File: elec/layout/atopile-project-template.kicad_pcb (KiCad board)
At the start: 2 copper layers, 1 part

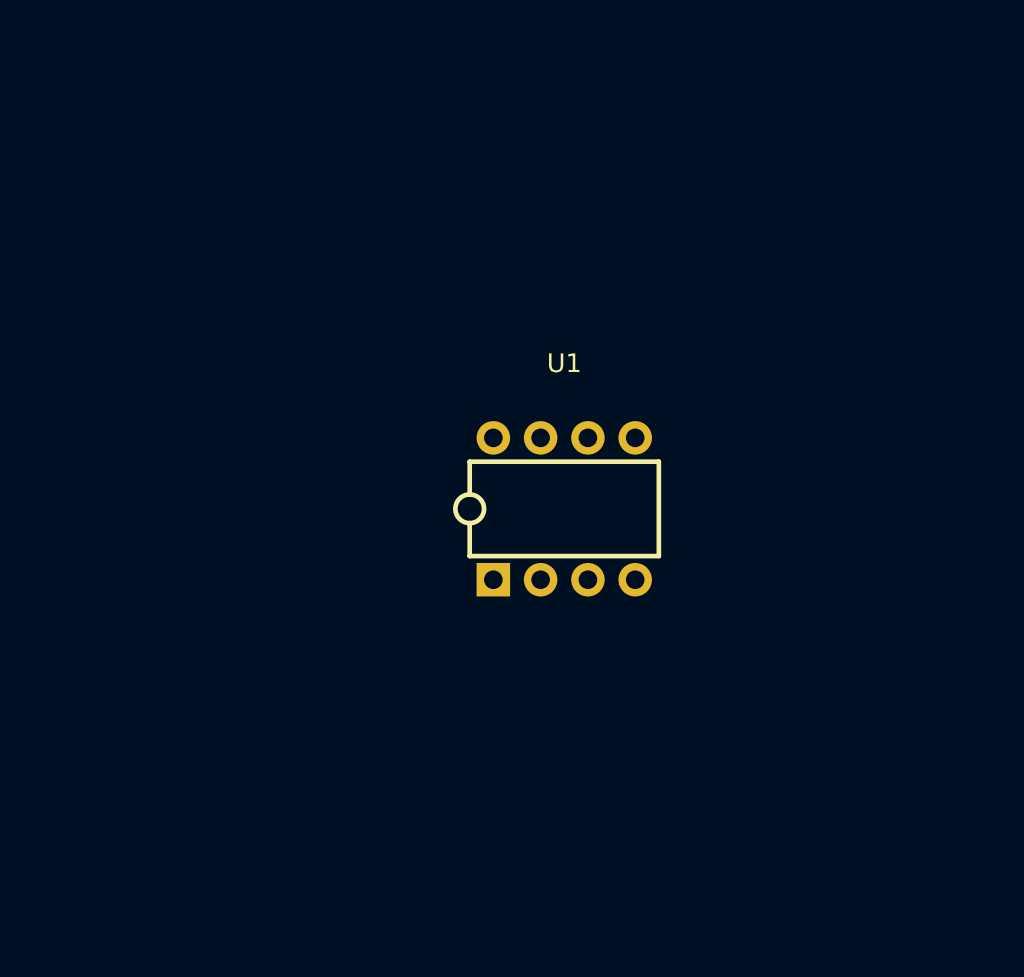
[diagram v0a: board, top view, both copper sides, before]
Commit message: added a few more comments, added a cap so we can show connections, modified kicad project lib path as it was broken
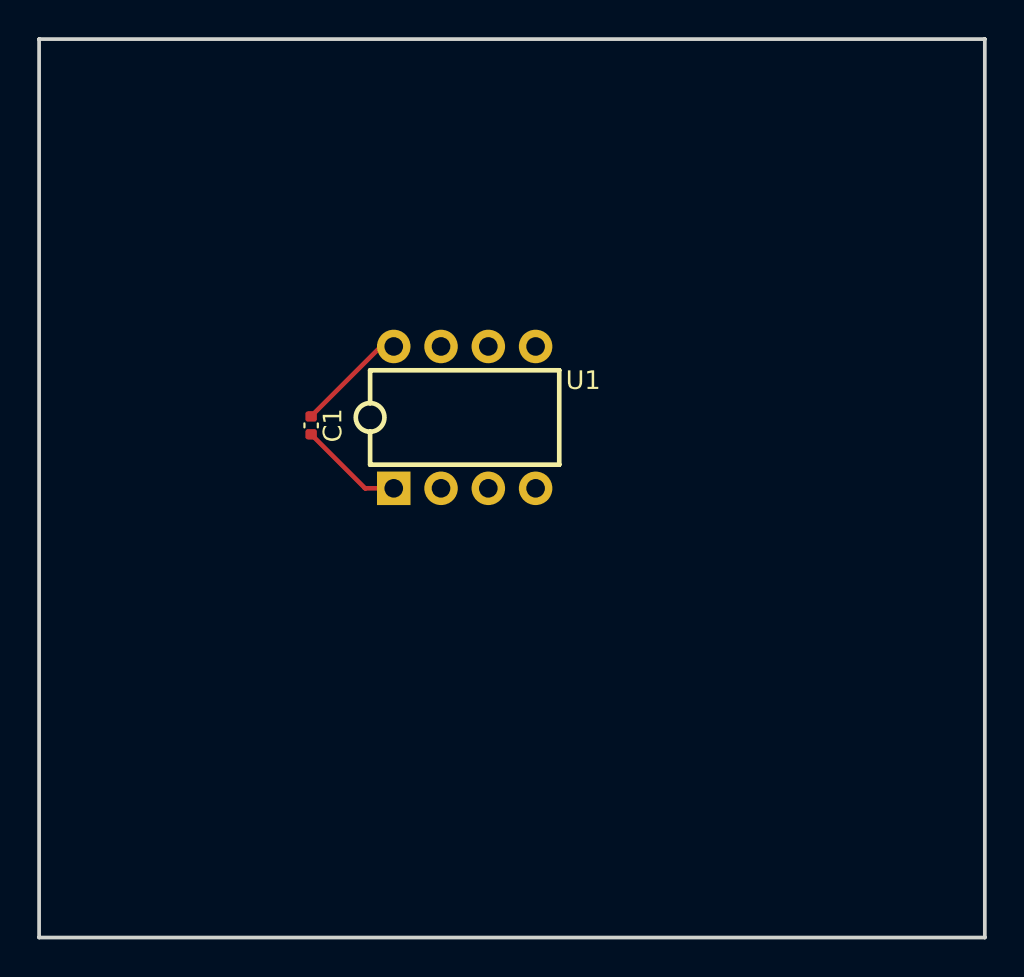
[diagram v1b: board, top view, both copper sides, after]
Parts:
- added C1: 100nF, Capacitor_SMD:C_0402_1005Metric, F.Cu at (134.0, 94.4)
- moved U1 7.26 mm to (142.2, 94.0)
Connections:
- U1 pad 1: Timer555-gnd -> HelloWorld-gnd
- U1 pad 8: Timer555-vcc_5v -> HelloWorld-vcc_5v
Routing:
- net HelloWorld-vcc_5v: track 0.00 -> 6.00 mm
- net HelloWorld-gnd: track 0.00 -> 5.64 mm
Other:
- board outline added: 50.8 x 48.3 mm
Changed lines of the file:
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@@
   )
   (net 0 "")
-  (net 1 "Timer555-gnd")
-  (net 2 "timer-trigger")
-  (net 3 "timer-output")
-  (net 4 "timer-reset")
-  (net 5 "timer-ctrl_v")
-  (net 6 "timer-threshold")
-  (net 7 "timer-discharge")
-  (net 8 "Timer555-vcc_5v")
+  (net 1 "HelloWorld-vcc_5v")
+  (net 2 "HelloWorld-gnd")
+  (net 3 "timer-trigger")
+  (net 4 "timer-output")
+  (net 5 "timer-reset")
+  (net 6 "timer-ctrl_v")
+  (net 7 "timer-threshold")
+  (net 8 "timer-discharge")
   (footprint "lib:DIP-8_L9.7-W6.4-P2.54-LS7.6-BL" (layer "F.Cu")
-    (at 147.59 98.89)
+    (at 142.24 93.98)
     (attr smd)
-    (fp_text reference "U1" (at 0 -7.81) (layer "F.SilkS")
+    (fp_text reference "U1" (at 6.363769 -1.989911) (layer "F.SilkS")
         (effects (font (size 1 1) (thickness 0.15)))
     )
@@
     (fp_line (start 5.08 2.54) (end 5.08 -2.53)
       (stroke (width 0.25) (type solid)) (layer "F.SilkS"))
-    (fp_arc (start -5.093438 0.769883) (mid -5.073311 -0.769971) (end -5.08 0.77)
+    (fp_arc (start -5.093438 0.769883) (mid -5.073281 -0.769971) (end -5.08 0.77)
       (stroke (width 0.25) (type solid)) (layer "F.SilkS"))
     (fp_circle (center -3.94 4.45) (end -3.64 4.45)
@@
       (stroke (width 0.06) (type solid)) (fill none) (layer "F.Fab"))
     (pad "1" thru_hole rect (at -3.81 3.81) (size 1.8 1.8) (drill 0.999998) (layers "*.Cu" "*.Mask")
-      (net 1 "Timer555-gnd"))
+      (net 2 "HelloWorld-gnd"))
     (pad "2" thru_hole circle (at -1.27 3.81) (size 1.8 1.8) (drill 0.999998) (layers "*.Cu" "*.Mask")
-      (net 2 "timer-trigger"))
+      (net 3 "timer-trigger"))
     (pad "3" thru_hole circle (at 1.27 3.81) (size 1.8 1.8) (drill 0.999998) (layers "*.Cu" "*.Mask")
-      (net 3 "timer-output"))
+      (net 4 "timer-output"))
     (pad "4" thru_hole circle (at 3.81 3.81) (size 1.8 1.8) (drill 0.999998) (layers "*.Cu" "*.Mask")
-      (net 4 "timer-reset"))
+      (net 5 "timer-reset"))
     (pad "5" thru_hole circle (at 3.81 -3.81) (size 1.8 1.8) (drill 0.999998) (layers "*.Cu" "*.Mask")
-      (net 5 "timer-ctrl_v"))
+      (net 6 "timer-ctrl_v"))
     (pad "6" thru_hole circle (at 1.27 -3.81) (size 1.8 1.8) (drill 0.999998) (layers "*.Cu" "*.Mask")
-      (net 6 "timer-threshold"))
+      (net 7 "timer-threshold"))
     (pad "7" thru_hole circle (at -1.27 -3.81) (size 1.8 1.8) (drill 0.999998) (layers "*.Cu" "*.Mask")
-      (net 7 "timer-discharge"))
+      (net 8 "timer-discharge"))
     (pad "8" thru_hole circle (at -3.81 -3.81) (size 1.8 1.8) (drill 0.999998) (layers "*.Cu" "*.Mask")
-      (net 8 "Timer555-vcc_5v"))
+      (net 1 "HelloWorld-vcc_5v"))
     (model "./lib/lib.3dshapes/DIP-8_L9.8-W6.6-H3.5-LS7.62-P2.54.wrl"
       (offset (xyz 0 -0 3))
@@
     )
   )
+  (footprint "Capacitor_SMD:C_0402_1005Metric" (layer "F.Cu")
+    (at 133.991711 94.410054 -90)
+    (descr "Capacitor SMD 0402 (1005 Metric), square (rectangular) end terminal, IPC_7351 nominal, (Body size source: IPC-SM-782 page 76, https://www.pcb-3d.com/wordpress/wp-content/uploads/ipc-sm-782a_amendment_1_and_2.pdf), generated with kicad-footprint-generator")
+    (tags "capacitor")
+    (attr smd)
+    (fp_text reference "C1" (at 0 -1.16 90) (layer "F.SilkS")
+        (effects (font (size 1 1) (thickness 0.15)))
+    )
+    (fp_text value "100nF" (at 0 1.16 90) (layer "F.Fab")
+        (effects (font (size 1 1) (thickness 0.15)))
+    )
+    (fp_text user "${REFERENCE}" (at 0 0 90) (layer "F.Fab")
+        (effects (font (size 0.25 0.25) (thickness 0.04)))
+    )
+    (fp_line (start -0.107836 -0.36) (end 0.107836 -0.36)
+      (stroke (width 0.12) (type solid)) (layer "F.SilkS"))
+    (fp_line (start -0.107836 0.36) (end 0.107836 0.36)
+      (stroke (width 0.12) (type solid)) (layer "F.SilkS"))
+    (fp_line (start -0.91 -0.46) (end 0.91 -0.46)
+      (stroke (width 0.05) (type solid)) (layer "F.CrtYd"))
+    (fp_line (start -0.91 0.46) (end -0.91 -0.46)
+      (stroke (width 0.05) (type solid)) (layer "F.CrtYd"))
+    (fp_line (start 0.91 -0.46) (end 0.91 0.46)
+      (stroke (width 0.05) (type solid)) (layer "F.CrtYd"))
+    (fp_line (start 0.91 0.46) (end -0.91 0.46)
+      (stroke (width 0.05) (type solid)) (layer "F.CrtYd"))
+    (fp_line (start -0.5 -0.25) (end 0.5 -0.25)
+      (stroke (width 0.1) (type solid)) (layer "F.Fab"))
+    (fp_line (start -0.5 0.25) (end -0.5 -0.25)
+      (stroke (width 0.1) (type solid)) (layer "F.Fab"))
+    (fp_line (start 0.5 -0.25) (end 0.5 0.25)
+      (stroke (width 0.1) (type solid)) (layer "F.Fab"))
+    (fp_line (start 0.5 0.25) (end -0.5 0.25)
+      (stroke (width 0.1) (type solid)) (layer "F.Fab"))
+    (pad "1" smd roundrect (at -0.48 0 270) (size 0.56 0.62) (layers "F.Cu" "F.Paste" "F.Mask") (roundrect_rratio 0.25)
+      (net 1 "HelloWorld-vcc_5v"))
+    (pad "2" smd roundrect (at 0.48 0 270) (size 0.56 0.62) (layers "F.Cu" "F.Paste" "F.Mask") (roundrect_rratio 0.25)
+      (net 2 "HelloWorld-gnd"))
+    (model "${KICAD6_3DMODEL_DIR}/Capacitor_SMD.3dshapes/C_0402_1005Metric.wrl"
+      (offset (xyz 0 0 0))
+      (scale (xyz 1 1 1))
+      (rotate (xyz 0 0 0))
+    )
+  )
+  (gr_rect (start 119.38 73.66) (end 170.18 121.92)
+    (stroke (width 0.2) (type default)) (fill none) (layer "Edge.Cuts"))
+  (segment (start 137.744156 90.17) (end 133.991711 93.922445) (width 0.25) (layer "F.Cu") (net 1))
+  (segment (start 133.991711 93.922445) (end 133.991711 93.930054) (width 0.25) (layer "F.Cu") (net 1))
+  (segment (start 138.43 90.17) (end 137.744156 90.17) (width 0.25) (layer "F.Cu") (net 1))
+  (segment (start 136.891657 97.79) (end 133.991711 94.890054) (width 0.25) (layer "F.Cu") (net 2))
+  (segment (start 138.43 97.79) (end 136.891657 97.79) (width 0.25) (layer "F.Cu") (net 2))
 )

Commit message: add mech folder and git hash
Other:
- board size 50.8 x 48.3 mm -> 40 x 40 mm
- board text added: "{{GITHASH}}"
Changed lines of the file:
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@@
     (fp_line (start 5.08 2.54) (end 5.08 -2.53)
       (stroke (width 0.25) (type solid)) (layer "F.SilkS"))
-    (fp_arc (start -5.093438 0.769883) (mid -5.073281 -0.769971) (end -5.08 0.77)
+    (fp_arc (start -5.093438 0.769883) (mid -5.073311 -0.769971) (end -5.08 0.77)
       (stroke (width 0.25) (type solid)) (layer "F.SilkS"))
     (fp_circle (center -3.94 4.45) (end -3.64 4.45)
@@
     )
   )
-  (gr_rect (start 119.38 73.66) (end 170.18 121.92)
-    (stroke (width 0.2) (type default)) (fill none) (layer "Edge.Cuts"))
+  (gr_line (start 123.2 113.4) (end 123.2 80.4)
+    (stroke (width 0.2) (type solid)) (layer "Edge.Cuts"))
+  (gr_arc (start 123.2 80.4) (mid 124.225126 77.925126) (end 126.7 76.9)
+    (stroke (width 0.2) (type solid)) (layer "Edge.Cuts"))
+  (gr_circle (center 159.7 80.4) (end 161.45 80.4)
+    (stroke (width 0.2) (type solid)) (fill none) (layer "Edge.Cuts"))
+  (gr_arc (start 159.7 76.9) (mid 162.174874 77.925126) (end 163.2 80.4)
+    (stroke (width 0.2) (type solid)) (layer "Edge.Cuts"))
+  (gr_line (start 163.2 113.4) (end 163.2 80.4)
+    (stroke (width 0.2) (type solid)) (layer "Edge.Cuts"))
+  (gr_arc (start 163.2 113.4) (mid 162.174874 115.874874) (end 159.7 116.9)
+    (stroke (width 0.2) (type solid)) (layer "Edge.Cuts"))
+  (gr_line (start 159.7 116.9) (end 126.7 116.9)
+    (stroke (width 0.2) (type solid)) (layer "Edge.Cuts"))
+  (gr_arc (start 159.7 76.9) (mid 162.174874 77.925126) (end 163.2 80.4)
+    (stroke (width 0.2) (type solid)) (layer "Edge.Cuts"))
+  (gr_arc (start 159.7 76.9) (mid 162.174874 77.925126) (end 163.2 80.4)
+    (stroke (width 0.2) (type solid)) (layer "Edge.Cuts"))
+  (gr_circle (center 126.7 113.4) (end 128.45 113.4)
+    (stroke (width 0.2) (type solid)) (fill none) (layer "Edge.Cuts"))
+  (gr_arc (start 163.2 113.4) (mid 162.174874 115.874874) (end 159.7 116.9)
+    (stroke (width 0.2) (type solid)) (layer "Edge.Cuts"))
+  (gr_arc (start 123.2 80.4) (mid 124.225126 77.925126) (end 126.7 76.9)
+    (stroke (width 0.2) (type solid)) (layer "Edge.Cuts"))
+  (gr_line (start 126.7 76.9) (end 159.7 76.9)
+    (stroke (width 0.2) (type solid)) (layer "Edge.Cuts"))
+  (gr_arc (start 126.7 116.9) (mid 124.225126 115.874874) (end 123.2 113.4)
+    (stroke (width 0.2) (type solid)) (layer "Edge.Cuts"))
+  (gr_line (start 163.2 80.4) (end 163.2 113.4)
+    (stroke (width 0.2) (type solid)) (layer "Edge.Cuts"))
+  (gr_arc (start 163.2 113.4) (mid 162.174874 115.874874) (end 159.7 116.9)
+    (stroke (width 0.2) (type solid)) (layer "Edge.Cuts"))
+  (gr_circle (center 159.7 113.4) (end 161.45 113.4)
+    (stroke (width 0.2) (type solid)) (fill none) (layer "Edge.Cuts"))
+  (gr_circle (center 126.7 80.4) (end 128.45 80.4)
+    (stroke (width 0.2) (type solid)) (fill none) (layer "Edge.Cuts"))
+  (gr_line (start 163.2 80.4) (end 163.2 113.4)
+    (stroke (width 0.2) (type solid)) (layer "Edge.Cuts"))
+  (gr_arc (start 126.7 116.9) (mid 124.225126 115.874874) (end 123.2 113.4)
+    (stroke (width 0.2) (type solid)) (layer "Edge.Cuts"))
+  (gr_circle (center 126.7 113.4) (end 128.45 113.4)
+    (stroke (width 0.2) (type solid)) (fill none) (layer "Edge.Cuts"))
+  (gr_circle (center 126.7 80.4) (end 128.45 80.4)
+    (stroke (width 0.2) (type solid)) (fill none) (layer "Edge.Cuts"))
+  (gr_circle (center 159.7 113.4) (end 161.45 113.4)
+    (stroke (width 0.2) (type solid)) (fill none) (layer "Edge.Cuts"))
+  (gr_arc (start 159.7 76.9) (mid 162.174874 77.925126) (end 163.2 80.4)
+    (stroke (width 0.2) (type solid)) (layer "Edge.Cuts"))
+  (gr_line (start 126.7 76.9) (end 159.7 76.9)
+    (stroke (width 0.2) (type solid)) (layer "Edge.Cuts"))
+  (gr_line (start 123.2 80.4) (end 123.2 113.4)
+    (stroke (width 0.2) (type solid)) (layer "Edge.Cuts"))
+  (gr_circle (center 126.7 113.4) (end 128.45 113.4)
+    (stroke (width 0.2) (type solid)) (fill none) (layer "Edge.Cuts"))
+  (gr_line (start 163.2 113.4) (end 163.2 80.4)
+    (stroke (width 0.2) (type solid)) (layer "Edge.Cuts"))
+  (gr_circle (center 126.7 80.4) (end 128.45 80.4)
+    (stroke (width 0.2) (type solid)) (fill none) (layer "Edge.Cuts"))
+  (gr_circle (center 159.7 113.4) (end 161.45 113.4)
+    (stroke (width 0.2) (type solid)) (fill none) (layer "Edge.Cuts"))
+  (gr_circle (center 126.7 80.4) (end 128.45 80.4)
+    (stroke (width 0.2) (type solid)) (fill none) (layer "Edge.Cuts"))
+  (gr_circle (center 126.7 113.4) (end 128.45 113.4)
+    (stroke (width 0.2) (type solid)) (fill none) (layer "Edge.Cuts"))
+  (gr_arc (start 126.7 116.9) (mid 124.225126 115.874874) (end 123.2 113.4)
+    (stroke (width 0.2) (type solid)) (layer "Edge.Cuts"))
+  (gr_line (start 123.2 80.4) (end 123.2 113.4)
+    (stroke (width 0.2) (type solid)) (layer "Edge.Cuts"))
+  (gr_circle (center 159.7 113.4) (end 161.45 113.4)
+    (stroke (width 0.2) (type solid)) (fill none) (layer "Edge.Cuts"))
+  (gr_arc (start 123.2 80.4) (mid 124.225126 77.925126) (end 126.7 76.9)
+    (stroke (width 0.2) (type solid)) (layer "Edge.Cuts"))
+  (gr_arc (start 163.2 113.4) (mid 162.174874 115.874874) (end 159.7 116.9)
+    (stroke (width 0.2) (type solid)) (layer "Edge.Cuts"))
+  (gr_line (start 159.7 116.9) (end 126.7 116.9)
+    (stroke (width 0.2) (type solid)) (layer "Edge.Cuts"))
+  (gr_line (start 126.7 116.9) (end 159.7 116.9)
+    (stroke (width 0.2) (type solid)) (layer "Edge.Cuts"))
+  (gr_line (start 126.7 116.9) (end 159.7 116.9)
+    (stroke (width 0.2) (type solid)) (layer "Edge.Cuts"))
+  (gr_circle (center 159.7 80.4) (end 161.45 80.4)
+    (stroke (width 0.2) (type solid)) (fill none) (layer "Edge.Cuts"))
+  (gr_arc (start 123.2 80.4) (mid 124.225126 77.925126) (end 126.7 76.9)
+    (stroke (width 0.2) (type solid)) (layer "Edge.Cuts"))
+  (gr_circle (center 159.7 80.4) (end 161.45 80.4)
+    (stroke (width 0.2) (type solid)) (fill none) (layer "Edge.Cuts"))
+  (gr_line (start 126.7 76.9) (end 159.7 76.9)
+    (stroke (width 0.2) (type solid)) (layer "Edge.Cuts"))
+  (gr_line (start 123.2 113.4) (end 123.2 80.4)
+    (stroke (width 0.2) (type solid)) (layer "Edge.Cuts"))
+  (gr_arc (start 126.7 116.9) (mid 124.225126 115.874874) (end 123.2 113.4)
+    (stroke (width 0.2) (type solid)) (layer "Edge.Cuts"))
+  (gr_line (start 126.7 76.9) (end 159.7 76.9)
+    (stroke (width 0.2) (type solid)) (layer "Edge.Cuts"))
+  (gr_circle (center 159.7 80.4) (end 161.45 80.4)
+    (stroke (width 0.2) (type solid)) (fill none) (layer "Edge.Cuts"))
+  (gr_text "{{GITHASH}} " (at 134.2 114.2) (layer "F.SilkS")
+    (effects (font (size 2 2) (thickness 0.1)) (justify left bottom))
+  )
   (segment (start 137.744156 90.17) (end 133.991711 93.922445) (width 0.25) (layer "F.Cu") (net 1))
   (segment (start 133.991711 93.922445) (end 133.991711 93.930054) (width 0.25) (layer "F.Cu") (net 1))
@@
   (segment (start 136.891657 97.79) (end 133.991711 94.890054) (width 0.25) (layer "F.Cu") (net 2))
   (segment (start 138.43 97.79) (end 136.891657 97.79) (width 0.25) (layer "F.Cu") (net 2))
+  (group "" (id 4e3ea3a3-d408-4ad8-873b-ebd87bd265e7)
+    (members
+      00e9e413-fe55-4320-b973-81fdf0b4cc24
+      0fc59361-2a09-4339-8464-495b51280d7e
+      12fa702a-45c0-4228-8798-0b1dff755467
+      1492c265-9600-4fac-807f-5aa558c04698
+      198da371-5ea4-4cce-89c6-a85e4e6fd5a2
+      20f5aec2-f82f-440a-88e0-7c770baed97c
+      23a80093-b831-494f-9bba-68421986c52c
+      26636bbf-1c2a-4df7-88c1-c20fa037cc7a
+      2b89afd7-dd24-41f4-85c0-9b0b291f5c57
+      2fc81b31-9add-483d-8263-1bf15a86faaf
+      34b8980e-5130-409d-83b7-73880c0817a4
+      36ab1010-5541-4b38-b363-4a27707f3202
+      3788308b-797f-4a53-8c52-00e61ef351dc
+      3a9095b0-7e4b-4c7f-aacb-bc9d3781fe0b
+      3d3db7c2-c89f-4be3-8e91-39fe7a9cebf3
+      3fee8cd8-9e80-4a1a-bcb8-484494266562
+      41a35e0c-0cd9-4884-83bf-a5f765917301
+      4354ef4b-af71-4b02-9a7b-930427945da3
+      4651f4aa-f85a-4992-9560-eff928a0e15f
+      4accd462-b544-44a7-ac19-ab4f0dd67dcb
+      4c413f87-443c-40db-810d-24d0127db4d1
+      55d6076c-5015-49df-810a-c55f5388576e
+      65b328d4-d955-42de-9ccd-564ff2e6e4da
+      65dc38af-d159-41f4-ba48-e112a9d8b717
+      69dabe7c-0c06-4af2-9c4e-d415cbc6d866
+      73c11e5d-a507-4a2f-8e42-2453482f9ba0
+      7609faaa-2ca7-4089-85bb-2ec6ff9f31bd
+      7dc85215-0547-4a98-92f9-7acc82968b0d
+      807b6513-e212-46b2-b774-80b1d14145d6
+      8278bfc6-c86b-4bbe-bee5-200ba347b53f
+      8adfd382-b7b3-40dc-abbc-698204ed259d
+      8d118edb-2a69-4839-a0e0-808db2b83267
+      9668049e-ace8-48bb-aaac-8c53c3bb8f64
+      abd0a840-cb12-4cfc-a11d-66180da66a73
+      ad767e51-32fc-4ffe-95cc-17d42beb101f
+      af147bb3-b7ba-4977-ab61-3eda152bc58e
+      b39eb833-0b6b-454c-91fa-8515f3b4c5a4
+      ba81428c-9237-4b33-8a8a-b0ef2c7129aa
+      bdb82cab-935c-4872-93ce-aa33a6ca8e3e
+      c200e945-b1eb-4ba9-846c-549b5888c1c9
+      c85d377d-8655-43a5-93e8-60ea0121da42
+      cdd996d3-1fa6-4070-aa95-b92a7005f8a0
+      db81513a-caef-41e6-97f5-8d6aa049d4d7
+      dbcff90b-bfca-4e87-8d37-d1133e183e20
+      e3c8b72a-7566-4951-ab61-af945b777583
+      e8b9d802-86fd-4393-87e2-6b6d02952d22
+      ec90ed93-4ada-407b-9626-0f35de0bac02
+      eeb07992-fe8e-4cf4-bf6c-0cf18fd77681
+    )
+  )
 )
